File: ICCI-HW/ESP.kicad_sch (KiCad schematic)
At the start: 5 parts

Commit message: updated
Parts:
- added C? (x5): 100n, symbol Device:C
- added J?: Conn_01x04, symbol Connector_Generic:Conn_01x04
- added R? (x2): 10k, symbol Device:R
- added R? (x4): 0R, symbol Device:R
- added SW?: SW_BOOT, symbol Switch:SW_Push
- added SW?: SW_RST_PROV, symbol Switch:SW_Push
- added SW?: SW_RST, symbol Switch:SW_Push
- added SW?: SW_LOG_SD, symbol Switch:SW_Push
- C?: value 100n -> 4.7u
- C?: value 22u -> 47u
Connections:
- net +3V3: now also C?.1, R?.2, R?.2, R?.2, R?.2
- net EN: now also C?.2, R?.1, SW?.1
- net GND: now also C?.1, C?.1, C?.1, C?.1, C?.2, SW?.2, SW?.2, SW?.2, SW?.2
- net TDI: now reaches U?.12 (IO27)
- net TDI: now also J?.2 (Pin_2)
- net TCK: now reaches U?.13 (IO14)
- net TCK: now also J?.3 (Pin_3)
- net TMS: now reaches U?.14 (IO12)
- net TMS: now also J?.1 (Pin_1)
- net TDO: now reaches U?.15 (GND)
- net TDO: now also J?.4 (Pin_4)
- net IO0: now reaches U?.25 (IO0)
- net IO0: now also C?.2, R?.1, SW?.1
- net RXD: now reaches U?.34 (RXD0)
- net RXD: now also R?.1, R?.2
- net TXD: now reaches U?.35 (TXD0)
- net TXD: now also R?.1, R?.2
- net IO33: no longer names the net of U?.9 (IO33)
- new net LOG_SD: C?.2, R?.1, SW?.1
- new net RST_PROV: C?.2, R?.1, SW?.1
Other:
- note added: "BUTTONS"
- note added: "Bootstrapping pins: MTDI (GPIO12) MTDO (GPIO15) BOOT (GPIO0) GPIO2 GPIO5"
- note added: "JTAG"
- moved on the sheet: C?, R?, U?

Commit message: updated
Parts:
- SW?: value SW_LOG_SD -> SW_LOG_SD_EN
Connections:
- net LOG_SD is gone; now on net LOG_EN: C?.2, R?.1, SW?.1
- net RST_PROV: now also U?.7 (IO35)
- net TCK: now also U?.16 (IO13); no longer U?.13 (IO14)
- net TDI: now also U?.14 (IO12); no longer U?.12 (IO27)
- net TDO: now also U?.23 (IO15); no longer U?.15 (GND)
- net TMS: now also U?.13 (IO14); no longer U?.14 (IO12)
- net SCL1: now reaches U?.10 (IO25)
- net SDA1: now reaches U?.11 (IO26)
- net VSPI_CLK: now reaches U?.30 (IO18)
- net VSPI_MISO: now reaches U?.31 (IO19)
- net LOG_EN: now reaches U?.33 (IO21)
- net ~{SD_CS}: now reaches U?.36 (IO22)
- net VSPI_MOSI: now reaches U?.37 (IO23)
- net SDA0: now reaches U?.8 (IO32)
- net DS_DQ: now reaches U?.9 (IO33)
- new net SCL0: U?.12 (IO27)
- no-connect marks 0 -> 9
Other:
- note added: "Bootstrapping pins: MTDI (GPIO12) MTDO (GPIO15) BOOT (GPIO0) GPIO2 GPIO5 GPIO34-35-36-37-38-39 Input only"
- note added: "SPI and UART direct I/O via I/O MUX while I2C and other low speed stuff can be mapped anywhere through GPIO Matrix. SPI, GPIO16, GPIO17 used by internal FLASH and PSRAM HSPI mapped on same pins of JTAG VSPI is free. SPID=MOSI SPIQ=MISO SPICLK=SPICLK SPIHD=Hold SPIWP=Write Protect WP & HD pin not used in SPI 1 bit mode"
- note removed: "Bootstrapping pins: MTDI (GPIO12) MTDO (GPIO15) BOOT (GPIO0) GPIO2 GPIO5"
- moved on the sheet: C?, R?

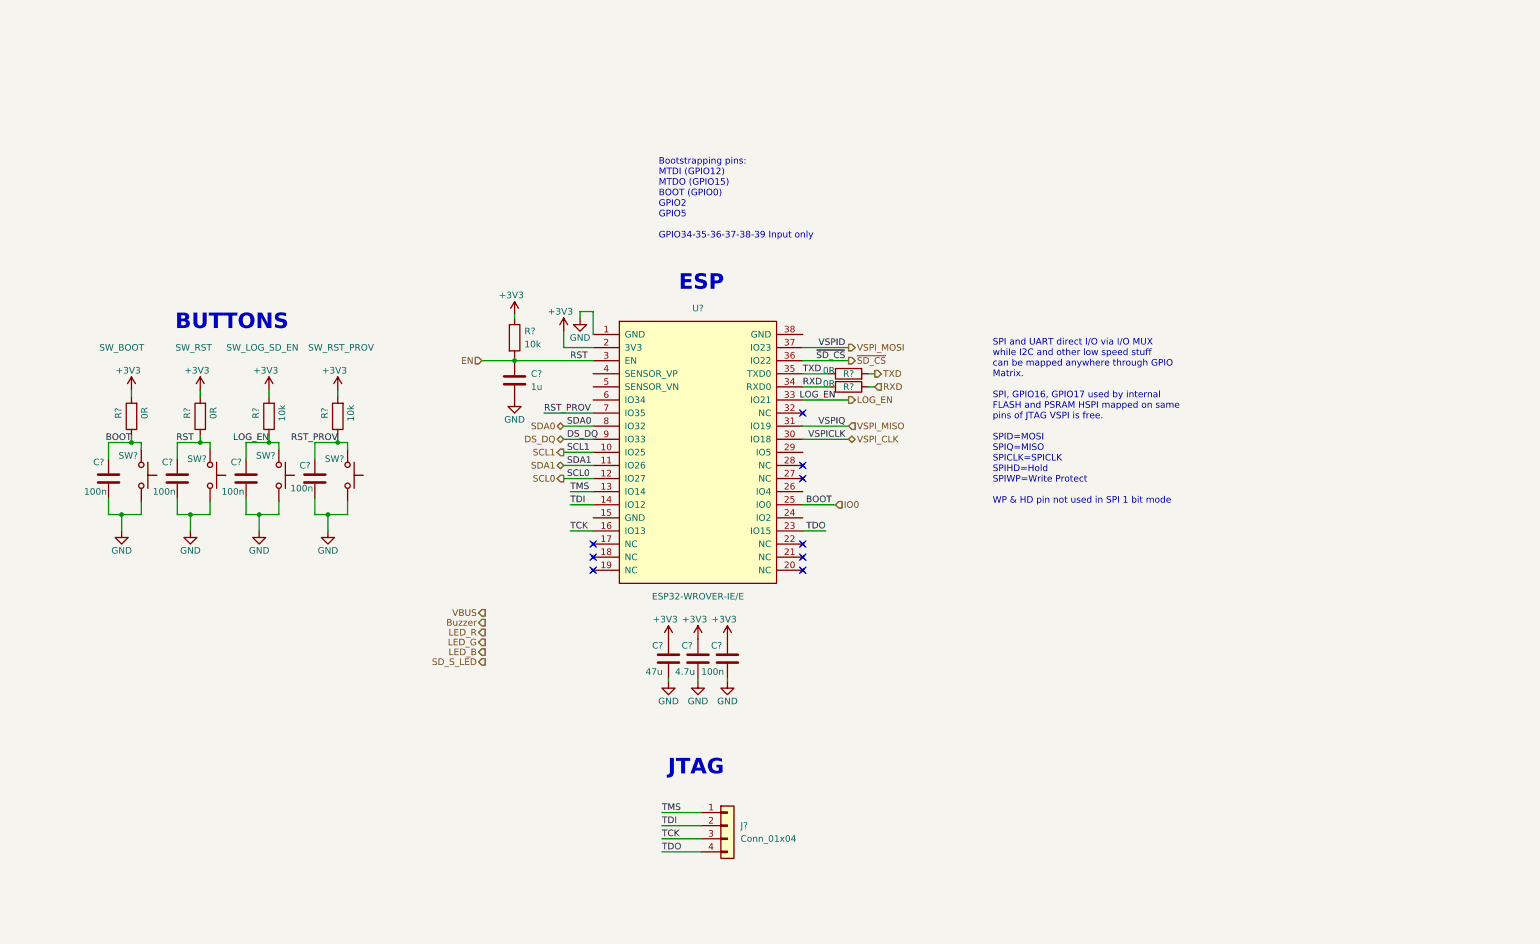
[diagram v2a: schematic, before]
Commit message: add GPIO Expansion
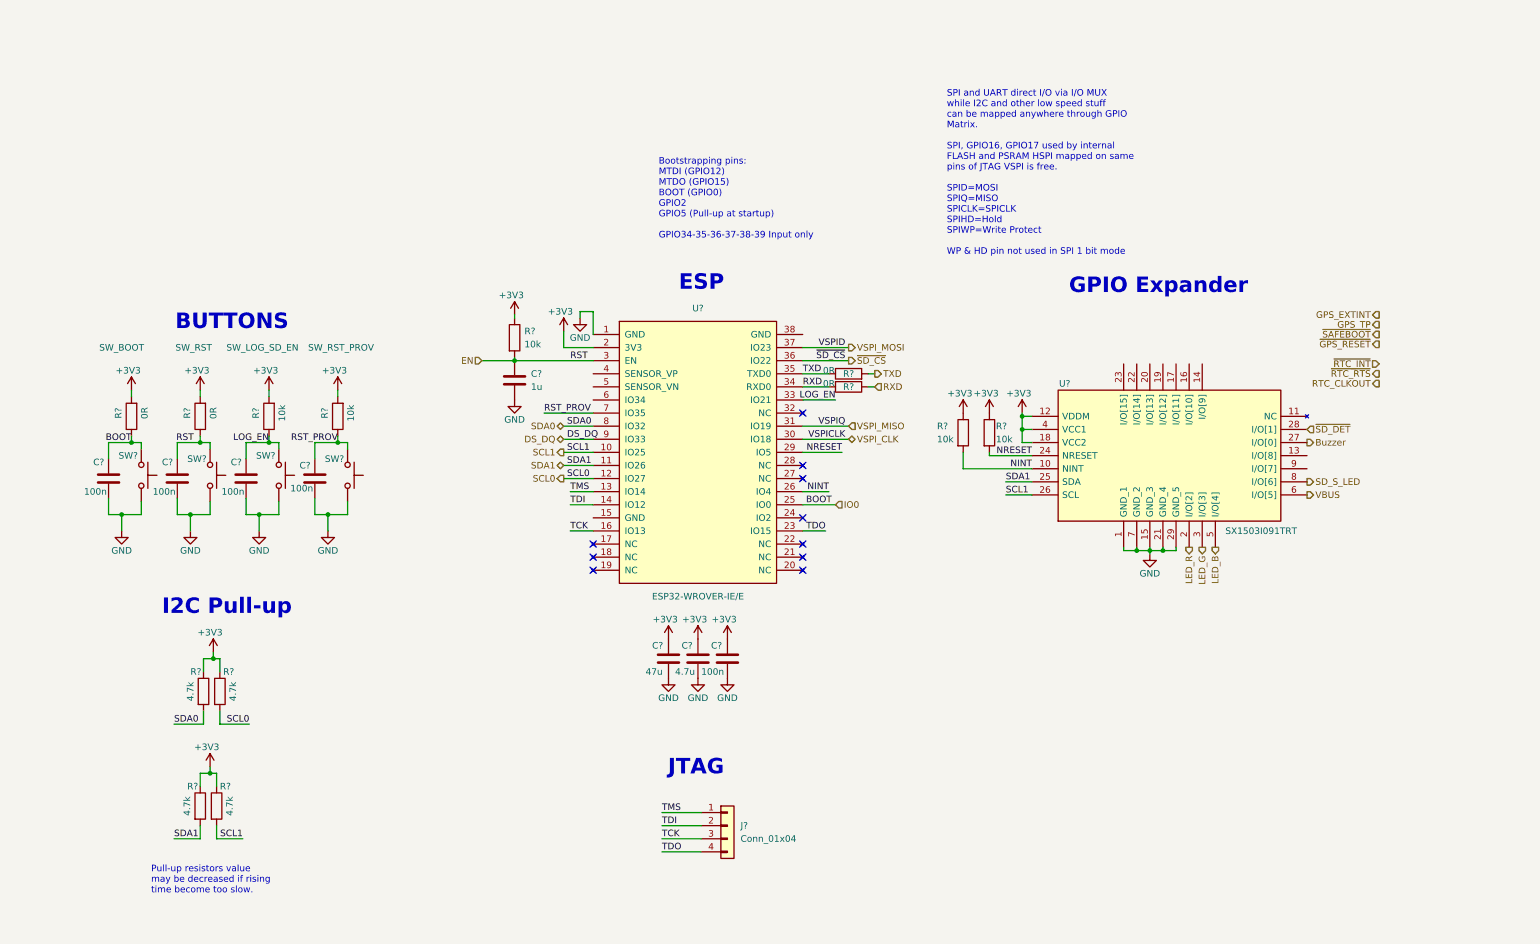
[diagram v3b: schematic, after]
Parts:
- added R? (x4): 4.7k, symbol Device:R
- added R? (x2): 10k, symbol Device:R
- added U?: SX1503I091TRT, symbol ICCI-LIB:SX1503I091TRT
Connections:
- net +3V3: now also R?.1, R?.1, R?.1, R?.1, R?.1, R?.1, U?.12 (VDDM), U?.18 (VCC2), U?.4 (VCC1)
- net Buzzer: now also U?.27 (I/O[0])
- net GND: now also U?.1 (GND_1), U?.15 (GND_3), U?.21 (GND_4), U?.29 (GND_5), U?.7 (GND_2)
- net LED_B: now also U?.5 (I/O[4])
- net LED_G: now also U?.3 (I/O[3])
- net LED_R: now also U?.2 (I/O[2])
- net SCL0: now also R?.2
- net SCL1: now also R?.2, U?.26 (SCL)
- net SDA0: now also R?.2
- net SDA1: now also R?.2, U?.25 (SDA)
- net SD_S_LED: now also U?.8 (I/O[6])
- net VBUS: now also U?.6 (I/O[5])
- net NINT: now reaches U?.26 (IO4)
- net NINT: now also R?.2, U?.10 (NINT)
- net NRESET: now reaches U?.29 (IO5)
- net NRESET: now also R?.2, U?.24 (NRESET)
- new net ~{SD_DET}: U?.28 (I/O[1])
- no-connect marks 9 -> 10
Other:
- note added: "Bootstrapping pins: MTDI (GPIO12) MTDO (GPIO15) BOOT (GPIO0) GPIO2 GPIO5 (Pull-up at startup) GPIO34-35-36-37-38-39 Input only"
- note added: "GPIO Expander"
- note added: "I2C Pull-up"
- note added: "Pull-up resistors value may be decreased if rising time become too slow."
- note removed: "Bootstrapping pins: MTDI (GPIO12) MTDO (GPIO15) BOOT (GPIO0) GPIO2 GPIO5 GPIO34-35-36-37-38-39 Input only"

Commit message: updated
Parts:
- added C?: 1n, symbol Device:C
- added C?: 100n, symbol Device:C
- added D?: DZ 3.3V 5mA, symbol Device:D_Zener
- added D?: UCLAMP3301D.TCT, symbol ICCI-LIB:TVS-Unidirectional
- added R?: 100k, symbol Device:R
- added R?: 200k, symbol Device:R
- added R?: 10k, symbol Device:R
- added SW?: RGB_CHRG, symbol Switch:SW_Push
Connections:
- net VBUS is gone; now on net LOG_EN: U?.6 (I/O[5])
- net +3V3: now also C?.2, D?.1, SW?.1
- net DS_DQ: now also U?.33 (IO21); no longer U?.9 (IO33)
- net GND: now also C?.2, D?.2, D?.2 (A), R?.2, R?.2
- net LOG_EN: no longer U?.33 (IO21)
- net NINT: now also U?.5 (SENSOR_VN); no longer U?.26 (IO4)
- net NRESET: now also U?.26 (IO4); no longer U?.29 (IO5)
- net MAX_INOKB: now reaches U?.13 (I/O[8])
- net CHREN: now reaches U?.14 (I/O[9])
- net CHR0: now reaches U?.16 (I/O[10])
- net CHR1: now reaches U?.17 (I/O[11])
- net ~{BATT_S_LED}: now reaches U?.9 (I/O[7])
- net VBAT_SENS: now reaches U?.4 (SENSOR_VP)
- net VBAT_SENS: now also C?.1, D?.1 (K), R?.1, R?.2
- net RGB_CHRG: now reaches U?.6 (IO34)
- net RGB_CHRG: now also C?.1, R?.1, SW?.2
- net SD_S_LED renamed ~{SD_S_LED}
- new net +BATT: R?.1
- new net MAX_INTB: U?.9 (IO33)
- no-connect marks 10 -> 11
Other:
- note added: "100mA"
- note added: "2V - 3V"
- note added: "500mA"
- note added: "6V - 9V"
- note added: "Depending on the I2C bus speed, these values may be decreased."
- note added: "EN/DIS uSD log"
- note added: "ESP Bootstrapping pins: MTDI (GPIO12) -> need to be kept low at startup: 0=LDO 3V3, 1=LDO 1V8 MTDO (GPIO15) -> 1=U0TXD Active 0=U0TXD Silent BOOT (GPIO0) -> 1=SPI, 0=Bootloader GPIO2 -> 0 for Bootloader mode GPIO5 (Pull-up at startup) SDIO timing"
- note added: "ESP boot mode"
- note added: "GPIO34-35-36-37-38-39 Input only"
- note added: "I/O 6,7,14,15 High Sink current 24mA. Other pins 12mA sink current. All pins 8mA source current."
- note added: "RTC PINS can receive interrupt and wake up ESP from deep-sleep. NINT, RGB, CHRG, RST PROV, MAX_INTB."
- note added: "Reset ESP"
- note added: "Reset provisioning"
- note added: "Show charging status on RGB Led for 5s"
- note added: "Since MTDI and MTDO are bootstrapping pins, wait for reset before using JTAG interface."
- note added: "Up to 1.5A (and maybe more?)"
- note removed: "Bootstrapping pins: MTDI (GPIO12) MTDO (GPIO15) BOOT (GPIO0) GPIO2 GPIO5 (Pull-up at startup) GPIO34-35-36-37-38-39 Input only"
- note removed: "Pull-up resistors value may be decreased if rising time become too slow."
- moved on the sheet: C?, J?, R?, SW?, U?

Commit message: schematic V1.0
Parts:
- removed C?: 100n, symbol Device:C
- removed SW?: RGB_CHRG, symbol Switch:SW_Push
- added C510, C511: 100n, symbol Device:C
- added R515: 10k, symbol Device:R
- added SW505: SW_RGB_CHRG, symbol Switch:SW_Push
- added SW506: SW_SLEEP, symbol Switch:SW_Push
- added TP501: TP_3V3, symbol Connector:TestPoint
- added TP502: TP_Li_Ion, symbol Connector:TestPoint
- added TP503: TP_VSYS, symbol Connector:TestPoint
- added TP504: TP_GND, symbol Connector:TestPoint
- added TP505: TP_3V_BAT, symbol Connector:TestPoint
- added TP506: TP_CLK/TP, symbol Connector:TestPoint
- added TP507: TP_VBUS, symbol Connector:TestPoint
- added TP508: TP_1V8, symbol Connector:TestPoint
- J501: renamed from J?; value Conn_01x04 -> JTAG
- gave numbers to parts that had none: 33
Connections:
- net +3V3: now also R512.1, R515.1, TP501.1
- net +BATT: now also TP502.1
- net Buzzer: now also U502.13 (I/O[8]); no longer U502.27 (I/O[0])
- net GND: now also U501.15 (GND), U501.38 (GND), C510.1, C511.1, SW505.2, SW506.2, TP504.1; no longer R512.2
- net LOG_EN: now also U502.27 (I/O[0]); no longer U502.6 (I/O[5])
- net MAX_INOKB: now also U502.9 (I/O[7]); no longer U502.13 (I/O[8])
- net RGB_CHRG: now also R512.2, U502.19 (I/O[12]), C510.2, SW505.1; no longer R512.1, U501.6 (IO34)
- net ~{BATT_S_LED}: now also U502.8 (I/O[6]); no longer U502.9 (I/O[7])
- net ~{SD_S_LED}: now also U502.6 (I/O[5]); no longer U502.8 (I/O[6])
- new net +1V8: TP508.1
- new net 3V_BAT: TP505.1
- new net SLEEP: C511.2, R515.2, SW506.1, U501.6 (IO34)
- new net VBUS: TP507.1
- new net VCC: TP503.1
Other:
- note added: "Depending on the I2C bus speed, these values may be decreased. 100KHz=4,7K 400KHz=2,2K"
- note added: "Sleep"
- note added: "Testpoints"
- note removed: "Depending on the I2C bus speed, these values may be decreased."
- moved on the sheet: C501, C503, C505, C506, R507, R508, R510, R511, R512, R513, R514, SW501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

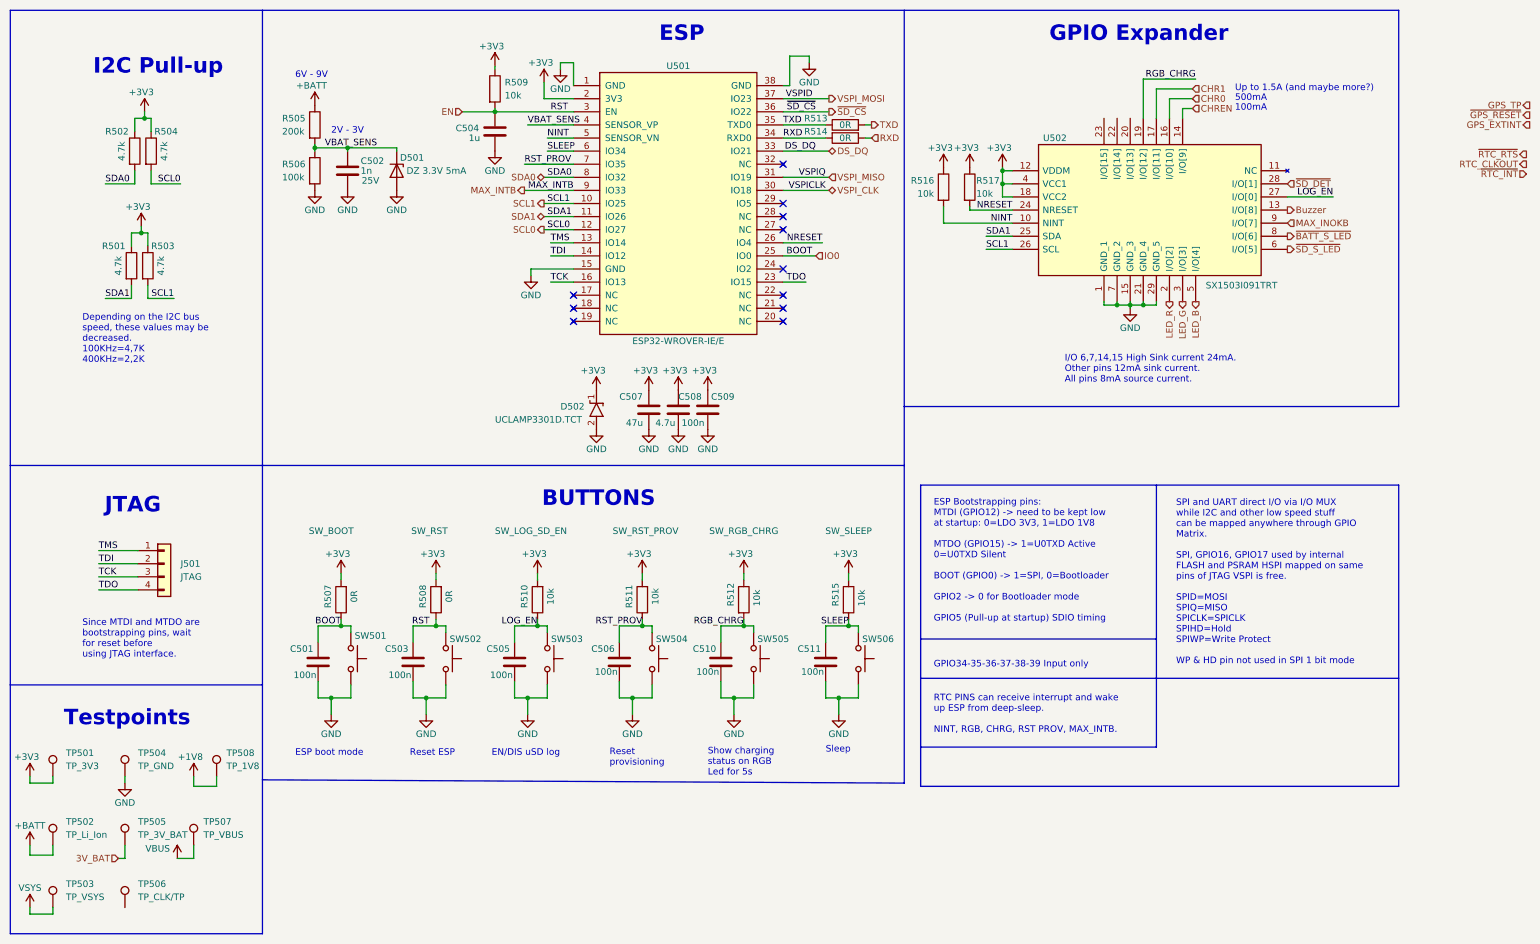
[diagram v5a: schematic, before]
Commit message: footprint assigned
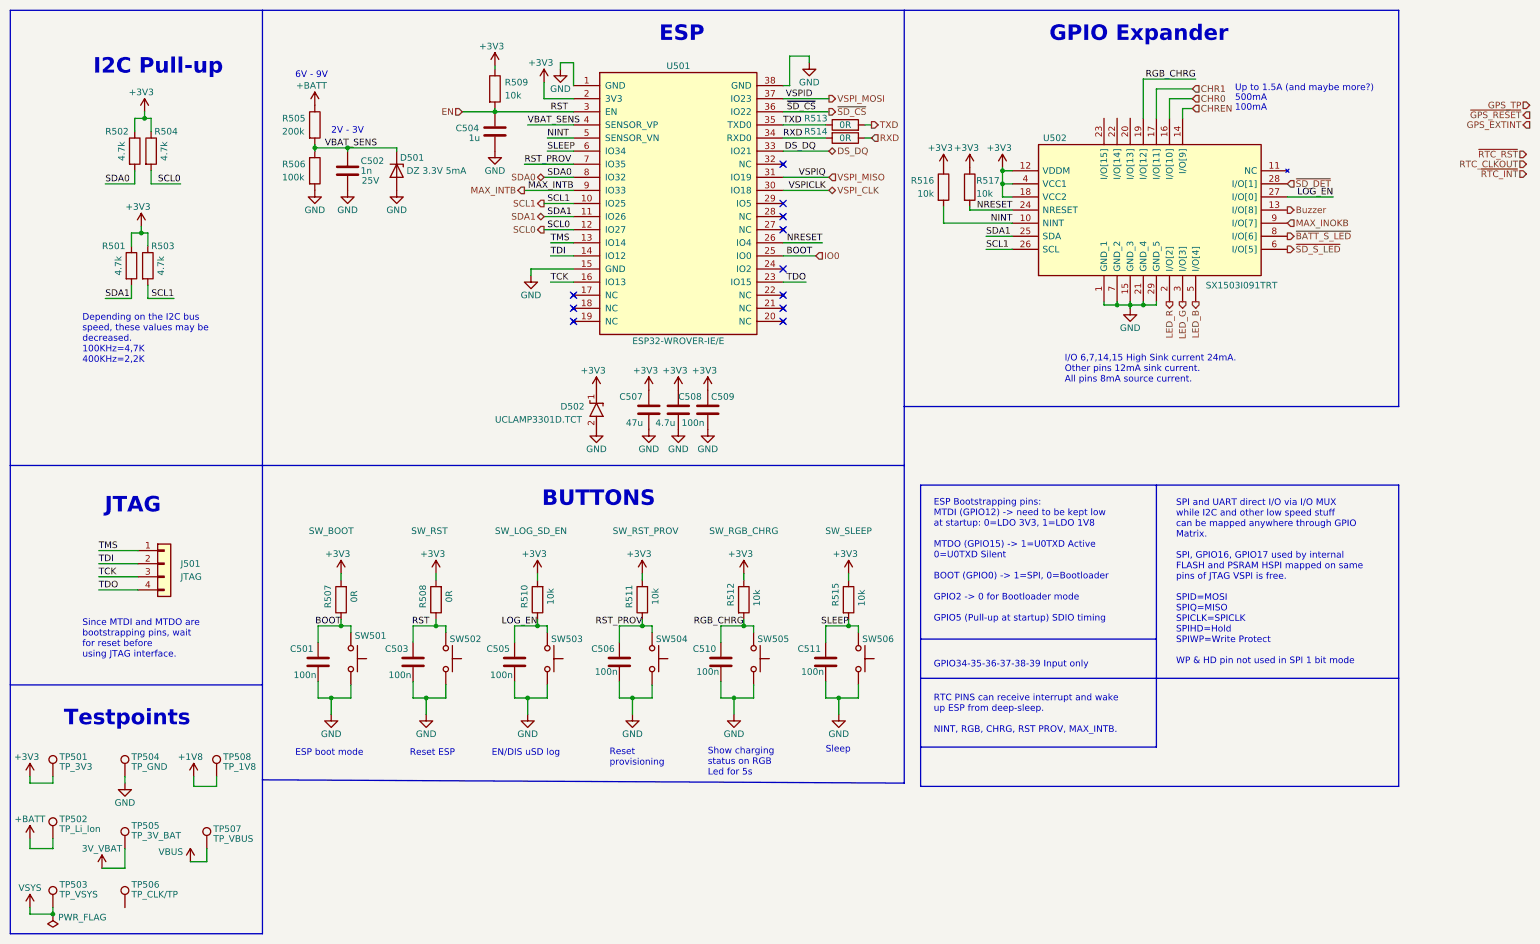
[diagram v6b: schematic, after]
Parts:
- C501, C502, C503, C504, C505, C506, C508, C509, C510, C511: footprint (none) -> Capacitor_SMD:C_0603_1608Metric
- C507: footprint (none) -> Capacitor_SMD:C_1210_3225Metric
- D501: footprint (none) -> Diode_SMD:D_SOD-923; Model SZ, NZ9F3V3ST5G -> NZ9F3V3ST5G
- D502: footprint (none) -> Diode_SMD:D_SOD-323
- J501: footprint (none) -> Connector_PinHeader_2.54mm:PinHeader_1x04_P2.54mm_Vertical
- R501, R502, R503, R504, R505, R506, R507, R508, R509, R510, R511, R512, R513, R514, R515, R516, R517: footprint (none) -> Resistor_SMD:R_0603_1608Metric
- SW501, SW502, SW503, SW504, SW505, SW506: footprint (none) -> Button_Switch_THT:SW_Tactile_SPST_Angled_PTS645Vx83-2LFS
- TP501, TP502, TP503, TP504, TP505, TP506, TP507, TP508: footprint (none) -> TestPoint:TestPoint_Plated_Hole_D2.0mm
- U501: footprint (none) -> ICCI-LIB:ESP32-WROVER-IE
- U502: footprint (none) -> ICCI-LIB:SX1503I091TRT
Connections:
- net 3V_BAT renamed +3V0
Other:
- moved on the sheet: TP502, TP505, TP507
